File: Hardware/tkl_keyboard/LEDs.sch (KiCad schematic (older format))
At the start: 206 parts

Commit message: Keyswitch, LED and diode placement done
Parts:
- added D193: K62, custom_footprint_library:SK6812-MINI-E, symbol custom_parts_library:SK68XX-MINI-E
- D11: value K76 -> K77
- D121: value K77 -> K78
- D123: value K65 -> K66
- D128: value K66 -> K67
- D131: value K78 -> K79
- D134: value K67 -> K68
- D139: value K68 -> K69
- D142: value K79 -> K80
- D145: value K69 -> K70
- D150: value K70 -> K71
- D153: value K80 -> K81
- D156: value K71 -> K72
- D159: value K81 -> K82
- D163: value K72 -> K73
- D166: value K82 -> K83
- D17: value K63 -> K64
- D170: value K73 -> K74
- D173: value K83 -> K84
- D177: value K74 -> K75
- D179: value K84 -> K85
- D184: value K85 -> K86
- D187: value K75 -> K76
- D188: value K86 -> K87
- D191: value K87 -> K88
- D25: value K64 -> K65
- D5: value K62 -> K63
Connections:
- net +5V: now also D193.1 (VDD)
- net GND: now also D193.3 (GND)
- net at D183.4 (DIN): now also D193.2 (DOUT); no longer D190.2 (DOUT)
- new net: D190.2 (DOUT), D193.4 (DIN)

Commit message: LEDs and diodes routed
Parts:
- D160: value UG_LED_12 -> UG_10
- D167: value UG_LED_13 -> UG_11
- D174: value UG_LED_14 -> UG_12
- D180: value UG_LED_15 -> UG_13
- D24: value UG_LED_6 -> UG_4
- D30: value UG_LED_7 -> UG_5
- D35: value UG_LED_2 -> UG_0
- D36: value UG_LED_8 -> UG_6
- D41: value UG_LED_3 -> UG_1
- D42: value UG_LED_9 -> UG_7
- D47: value UG_LED_4 -> UG_2
- D48: value UG_LED_10 -> UG_8
- D49: value UG_LED_5 -> UG_3
- D50: value UG_LED_11 -> UG_9
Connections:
- net at D178.4 (DIN): now also D190.2 (DOUT); no longer D183.2 (DOUT)
- net at D183.4 (DIN): now also D37.2 (DOUT); no longer D193.2 (DOUT)
- net at D186.4 (DIN): now also D193.2 (DOUT); no longer D182.2 (DOUT)
- net at D193.4 (DIN): now also D182.2 (DOUT); no longer D190.2 (DOUT)
- net at D31.4 (DIN): now also D183.2 (DOUT); no longer D37.2 (DOUT)
- net at D25.4 (DIN): now also D5.2 (DOUT); no longer D17.2 (DOUT)
- net at D17.4 (DIN): now also D121.2 (DOUT); no longer D5.2 (DOUT)
- net at D11.4 (DIN): now also D17.2 (DOUT); no longer D121.2 (DOUT)
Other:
- moved on the sheet: D17, D183, D186, D19, D190, D193, D26

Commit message: Rows and columns routed to controller. Extended top board edge to fit OLED. Removed optional resistors around CMC.
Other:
- moved on the sheet: C10, C100, C101, C102, C103, C104, C105, C106, C107, C108, C109, C11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

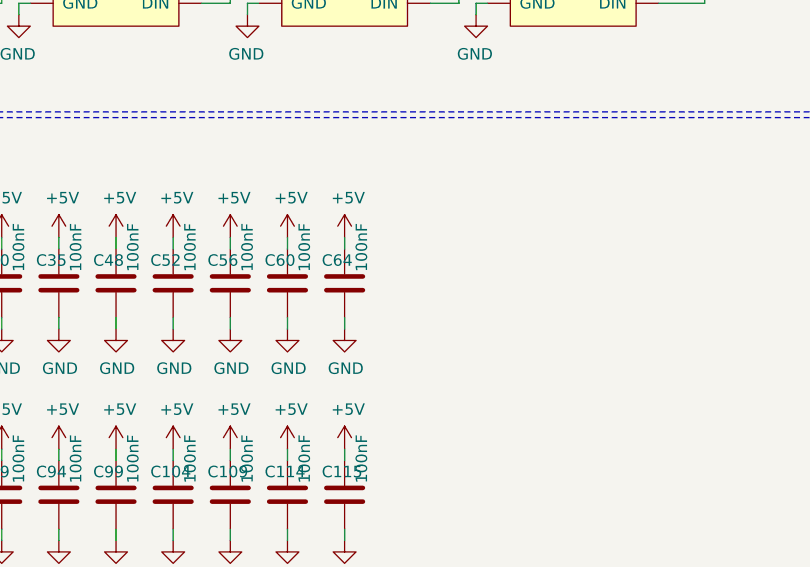
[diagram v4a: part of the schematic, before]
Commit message: Added some missing capacitors, Fixed DC jack footprint connections
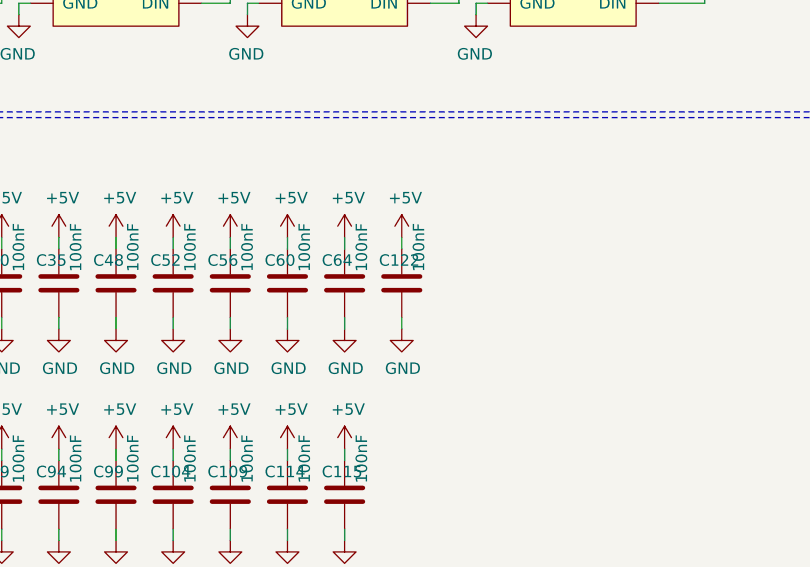
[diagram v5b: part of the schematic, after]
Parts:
- added C122: 100nF, Capacitor_smd:C_0603_1608Metric, symbol Device:C
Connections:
- net +5V: now also C122.1
- net GND: now also C122.2
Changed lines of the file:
@@
 $EndComp
 $Comp
-L Device:C C?
-U 1 1 649DA295
-P 13250 11575
-AR Path="/649DA295" Ref="C?"  Part="1"
-AR Path="/60D44BDB/649DA295" Ref="C?"  Part="1"
-AR Path="/60D99CF5/649DA295" Ref="C?"  Part="1"
-AR Path="/60D44364/649DA295" Ref="C?"  Part="1"
-AR Path="/61150193/649DA295" Ref="C?"  Part="1"
-AR Path="/61D5AB4C/649DA295" Ref="C?"  Part="1"
-AR Path="/61234213/649DA295" Ref="C?"  Part="1"
-AR Path="/62FB59AD/649DA295" Ref="C72"  Part="1"
-F 0 "C72" H 13150 11675 50  0000 L CNN
-F 1 "100nF" V 13325 11625 50  0000 L CNN
-F 2 "Capacitor_smd:C_0603_1608Metric" H 13288 11425 50  0001 C CNN
-F 3 "~" H 13250 11575 50  0001 C CNN
-	1    13250 11575
-	1    0    0    -1
-$EndComp
-$Comp
 L power:+5V #PWR?
 U 1 1 649DA29B
@@
 Wire Notes Line
 	3000 3000 20675 3000
+$Comp
+L Device:C C?
+U 1 1 649DA295
+P 13250 11575
+AR Path="/649DA295" Ref="C?"  Part="1"
+AR Path="/60D44BDB/649DA295" Ref="C?"  Part="1"
+AR Path="/60D99CF5/649DA295" Ref="C?"  Part="1"
+AR Path="/60D44364/649DA295" Ref="C?"  Part="1"
+AR Path="/61150193/649DA295" Ref="C?"  Part="1"
+AR Path="/61D5AB4C/649DA295" Ref="C?"  Part="1"
+AR Path="/61234213/649DA295" Ref="C?"  Part="1"
+AR Path="/62FB59AD/649DA295" Ref="C72"  Part="1"
+F 0 "C72" H 13150 11675 50  0000 L CNN
+F 1 "100nF" V 13325 11625 50  0000 L CNN
+F 2 "Capacitor_smd:C_0603_1608Metric" H 13288 11425 50  0001 C CNN
+F 3 "~" H 13250 11575 50  0001 C CNN
+	1    13250 11575
+	1    0    0    -1
+$EndComp
+$Comp
+L power:+5V #PWR?
+U 1 1 615F41BA
+P 18250 11375
+AR Path="/615F41BA" Ref="#PWR?"  Part="1"
+AR Path="/60D44BDB/615F41BA" Ref="#PWR?"  Part="1"
+AR Path="/60D99CF5/615F41BA" Ref="#PWR?"  Part="1"
+AR Path="/60D44364/615F41BA" Ref="#PWR?"  Part="1"
+AR Path="/61150193/615F41BA" Ref="#PWR?"  Part="1"
+AR Path="/61D5AB4C/615F41BA" Ref="#PWR?"  Part="1"
+AR Path="/61234213/615F41BA" Ref="#PWR?"  Part="1"
+AR Path="/62FB59AD/615F41BA" Ref="#PWR0193"  Part="1"
+F 0 "#PWR0193" H 18250 11225 50  0001 C CNN
+F 1 "+5V" H 18265 11548 50  0000 C CNN
+F 2 "" H 18250 11375 50  0001 C CNN
+F 3 "" H 18250 11375 50  0001 C CNN
+	1    18250 11375
+	1    0    0    -1
+$EndComp
+Wire Wire Line
+	18250 11425 18250 11375
+Wire Wire Line
+	18250 11725 18250 11775
+$Comp
+L power:GND #PWR?
+U 1 1 615F41C2
+P 18250 11775
+AR Path="/615F41C2" Ref="#PWR?"  Part="1"
+AR Path="/60D44BDB/615F41C2" Ref="#PWR?"  Part="1"
+AR Path="/60D99CF5/615F41C2" Ref="#PWR?"  Part="1"
+AR Path="/60D44364/615F41C2" Ref="#PWR?"  Part="1"
+AR Path="/61150193/615F41C2" Ref="#PWR?"  Part="1"
+AR Path="/61D5AB4C/615F41C2" Ref="#PWR?"  Part="1"
+AR Path="/61234213/615F41C2" Ref="#PWR?"  Part="1"
+AR Path="/62FB59AD/615F41C2" Ref="#PWR0522"  Part="1"
+F 0 "#PWR0522" H 18250 11525 50  0001 C CNN
+F 1 "GND" H 18255 11602 50  0000 C CNN
+F 2 "" H 18250 11775 50  0001 C CNN
+F 3 "" H 18250 11775 50  0001 C CNN
+	1    18250 11775
+	1    0    0    -1
+$EndComp
+$Comp
+L Device:C C?
+U 1 1 615F41C8
+P 18250 11575
+AR Path="/615F41C8" Ref="C?"  Part="1"
+AR Path="/60D44BDB/615F41C8" Ref="C?"  Part="1"
+AR Path="/60D99CF5/615F41C8" Ref="C?"  Part="1"
+AR Path="/60D44364/615F41C8" Ref="C?"  Part="1"
+AR Path="/61150193/615F41C8" Ref="C?"  Part="1"
+AR Path="/61D5AB4C/615F41C8" Ref="C?"  Part="1"
+AR Path="/61234213/615F41C8" Ref="C?"  Part="1"
+AR Path="/62FB59AD/615F41C8" Ref="C122"  Part="1"
+F 0 "C122" H 18150 11675 50  0000 L CNN
+F 1 "100nF" V 18325 11625 50  0000 L CNN
+F 2 "Capacitor_smd:C_0603_1608Metric" H 18288 11425 50  0001 C CNN
+F 3 "~" H 18250 11575 50  0001 C CNN
+	1    18250 11575
+	1    0    0    -1
+$EndComp
 $EndSCHEMATC
